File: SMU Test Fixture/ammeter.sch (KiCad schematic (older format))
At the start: 43 parts, among them K10 Sense Select, K5 Integrator Reset, K6 I/V Mode Select, K7 3x Gain Enable, K8 Shunt Select, K9 Shunt/Sense Select, U1 OPA192, U2 OPA189, U3 OPA551U, U4 OPA192, U5 OPA189, U6 OPA1611

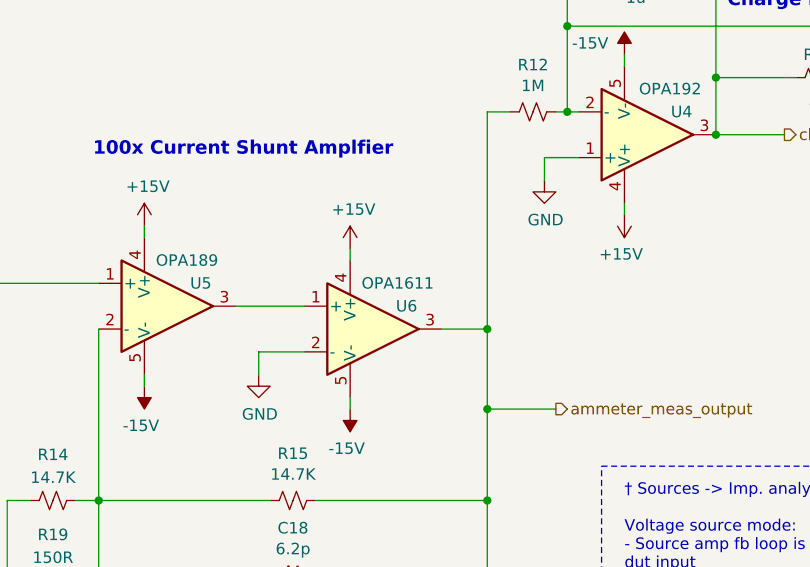
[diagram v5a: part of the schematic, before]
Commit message: Switch to opa1622 for greater stability.
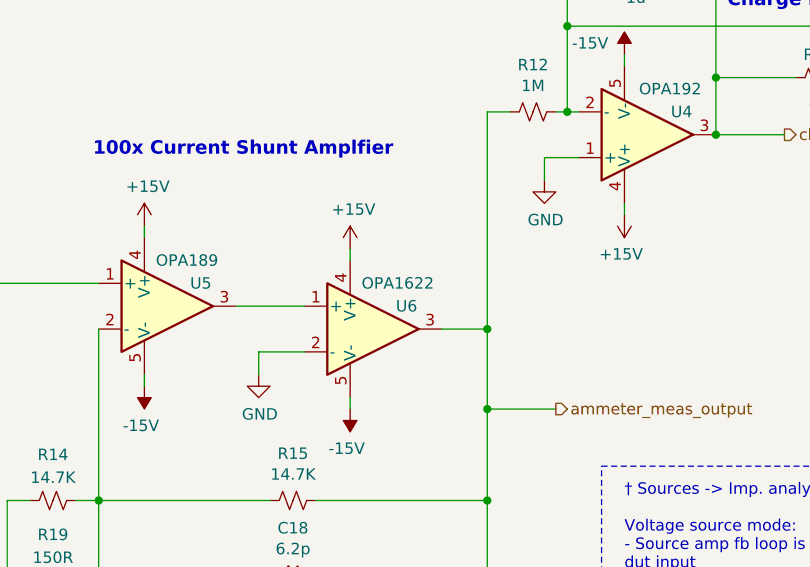
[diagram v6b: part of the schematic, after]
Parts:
- U6: value OPA1611 -> OPA1622; footprint Package_SO:SOIC-8_3.9x4.9mm_P1.27mm -> Package_SON:VSON-10-1EP_3x3mm_P0.5mm_EP1.2x2mm; PN OPA1611AIDR -> OPA1622
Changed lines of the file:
@@
 P 7400 4850
 F 0 "U6" H 7500 4950 50  0000 L CNN
-F 1 "OPA1611" H 7350 5050 50  0000 L CNN
-F 2 "Package_SO:SOIC-8_3.9x4.9mm_P1.27mm" H 7400 4850 50  0001 C CNN
-F 3 "https://www.ti.com/lit/ds/symlink/opa1611.pdf?HQS=TI-null-null-mousermode-df-pf-null-wwe&ts=1605474705530&ref_url=https%253A%252F%252Fwww.mouser.com%252F" H 7400 4850 50  0001 C CNN
-F 4 "OPA1611AIDR " H 7400 4850 50  0001 C CNN "PN"
+F 1 "OPA1622" H 7350 5050 50  0000 L CNN
+F 2 "Package_SON:VSON-10-1EP_3x3mm_P0.5mm_EP1.2x2mm" H 7400 4850 50  0001 C CNN
+F 3 "https://www.ti.com/lit/gpn/opa1622" H 7400 4850 50  0001 C CNN
+F 4 "OPA1622" H 7400 4850 50  0001 C CNN "PN"
 	1    7400 4850
 	1    0    0    -1

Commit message: Fix symbols for OPA189 and 192.
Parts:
- U1, U4: value OPA192 -> OPA192IDBVx; symbol pspice:OPAMP -> MAGI_Symbols:OPA192IDBVx
- U2, U5: value OPA189 -> OPA189IDBVx; footprint Package_TO_SOT_SMD:SOT-23-5_HandSoldering -> Package_TO_SOT_SMD:SOT-223-5; symbol pspice:OPAMP -> MAGI_Symbols:OPA189IDBVx
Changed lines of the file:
@@
 	1000 1100 1000 1200
 $Comp
-L pspice:OPAMP U4
+L MAGI_Symbols:OPA192IDBVx U4
 U 1 1 5FBD0B5D
 P 8600 4000
 F 0 "U4" H 8750 3900 50  0000 C CNN
-F 1 "OPA192" H 8700 3800 50  0000 C CNN
+F 1 "OPA192IDBVx" H 8900 4175 50  0000 C CNN
 F 2 "Package_TO_SOT_SMD:SOT-23-5_HandSoldering" H 8600 4000 50  0001 C CNN
-F 3 "https://www.ti.com/lit/ds/symlink/opa192.pdf?HQS=TI-null-null-mousermode-df-pf-null-wwe&ts=1605478144919&ref_url=https%253A%252F%252Fwww.mouser.com%252F" H 8600 4000 50  0001 C CNN
+F 3 "https://www.ti.com/lit/ds/symlink/opa192.pdf?ts=1616148990548" H 8600 4000 50  0001 C CNN
 F 4 "OPA192IDBVR" H 8600 4000 50  0001 C CNN "PN"
 	1    8600 4000
@@
 	10975 2850 10975 2650
 $Comp
-L pspice:OPAMP U1
+L MAGI_Symbols:OPA192IDBVx U1
 U 1 1 60366EC0
 P 8550 2550
@@
 AR Path="/6012FE35/60366EC0" Ref="U?"  Part="1"
 F 0 "U1" H 8700 2450 50  0000 C CNN
-F 1 "OPA192" H 8650 2350 50  0000 C CNN
+F 1 "OPA192IDBVx" H 8850 2725 50  0000 C CNN
 F 2 "Package_TO_SOT_SMD:SOT-23-5_HandSoldering" H 8550 2550 50  0001 C CNN
-F 3 "https://www.ti.com/lit/ds/symlink/opa192.pdf?HQS=TI-null-null-mousermode-df-pf-null-wwe&ts=1605478144919&ref_url=https%253A%252F%252Fwww.mouser.com%252F" H 8550 2550 50  0001 C CNN
+F 3 "https://www.ti.com/lit/ds/symlink/opa192.pdf?ts=1616148990548" H 8550 2550 50  0001 C CNN
 F 4 "OPA192IDBVR" H 8550 2550 50  0001 C CNN "PN"
 	1    8550 2550
@@
 	2150 3200 2200 3200
 $Comp
-L pspice:OPAMP U2
+L MAGI_Symbols:OPA189IDBVx U2
 U 1 1 60366F19
 P 2500 3100
@@
 AR Path="/6012FE35/60366F19" Ref="U?"  Part="1"
 F 0 "U2" H 2600 3200 50  0000 L CNN
-F 1 "OPA189" H 2450 3300 50  0000 L CNN
-F 2 "Package_TO_SOT_SMD:SOT-23-5_HandSoldering" H 2500 3100 50  0001 C CNN
-F 3 "https://www.ti.com/lit/gpn/opa189" H 2500 3100 50  0001 C CNN
+F 1 "OPA189IDBVx" H 2450 3300 50  0000 L CNN
+F 2 "Package_TO_SOT_SMD:SOT-223-5" H 2500 3100 50  0001 C CNN
+F 3 "https://www.ti.com/lit/ds/symlink/opa189.pdf" H 2500 3100 50  0001 C CNN
 F 4 "OPA189IDBVR" H 2500 3100 50  0001 C CNN "PN"
 	1    2500 3100
@@
 ammeter_meas_output
 $Comp
-L pspice:OPAMP U5
+L MAGI_Symbols:OPA189IDBVx U5
 U 1 1 5FAFE6A7
 P 6500 4750
 F 0 "U5" H 6600 4850 50  0000 L CNN
-F 1 "OPA189" H 6450 4950 50  0000 L CNN
-F 2 "Package_TO_SOT_SMD:SOT-23-5_HandSoldering" H 6500 4750 50  0001 C CNN
-F 3 "https://www.ti.com/lit/gpn/opa189" H 6500 4750 50  0001 C CNN
+F 1 "OPA189IDBVx" H 6450 4950 50  0000 L CNN
+F 2 "Package_TO_SOT_SMD:SOT-223-5" H 6500 4750 50  0001 C CNN
+F 3 "https://www.ti.com/lit/ds/symlink/opa189.pdf" H 6500 4750 50  0001 C CNN
 F 4 "OPA189IDBVR" H 6500 4750 50  0001 C CNN "PN"
 	1    6500 4750
